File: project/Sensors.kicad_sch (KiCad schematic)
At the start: 19 parts, among them IC201 APDS-9306-065, IC202 BMI270, IC203 BMP581, IC204 LIS2MDLTR, IC205 BME688, Q201 DMG1013UW-7

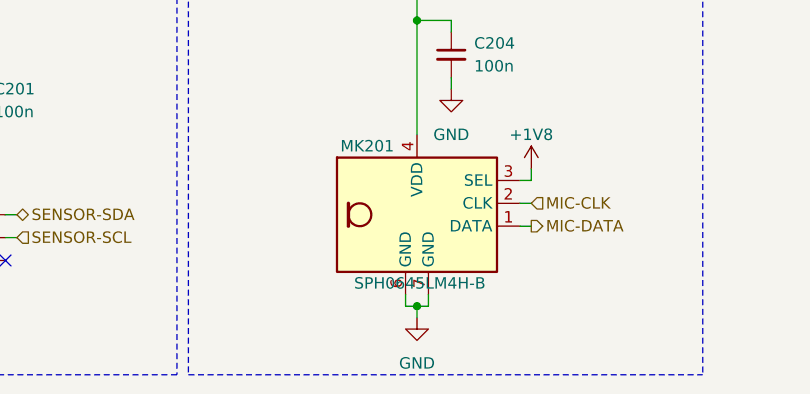
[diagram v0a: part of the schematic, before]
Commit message: Fix wrong value and datasheet for microphone
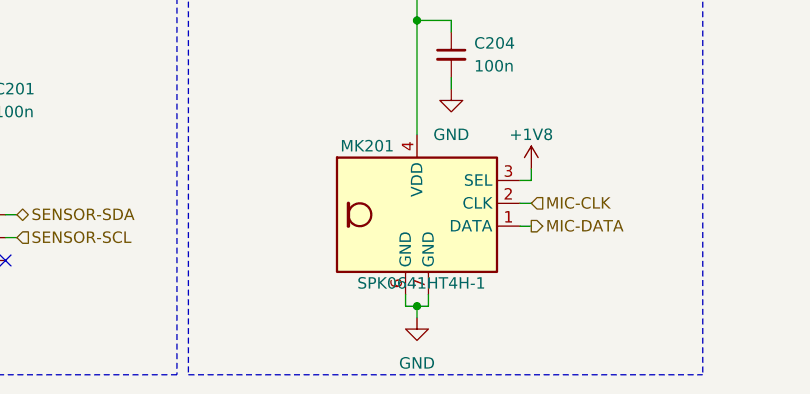
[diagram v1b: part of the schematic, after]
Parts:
- MK201: value SPH0645LM4H-B -> SPK0641HT4H-1
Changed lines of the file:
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@@
       (effects (font (size 1.27 1.27)) (justify right))
     )
-    (property "Value" "SPH0645LM4H-B" (at 87.63 186.69 0)
+    (property "Value" "SPK0641HT4H-1" (at 87.63 186.69 0)
       (effects (font (size 1.27 1.27)) (justify right))
     )
@@
       (effects (font (size 1.27 1.27)) hide)
     )
-    (property "Datasheet" "https://www.knowles.com/docs/default-source/default-document-library/sph0645lm4h-1-datasheet.pdf" (at 80.01 179.07 0)
+    (property "Datasheet" "https://www.knowles.com/docs/default-source/model-downloads/spk0641ht4h-1-rev-a.pdf" (at 80.01 179.07 0)
       (effects (font (size 1.27 1.27)) hide)
     )

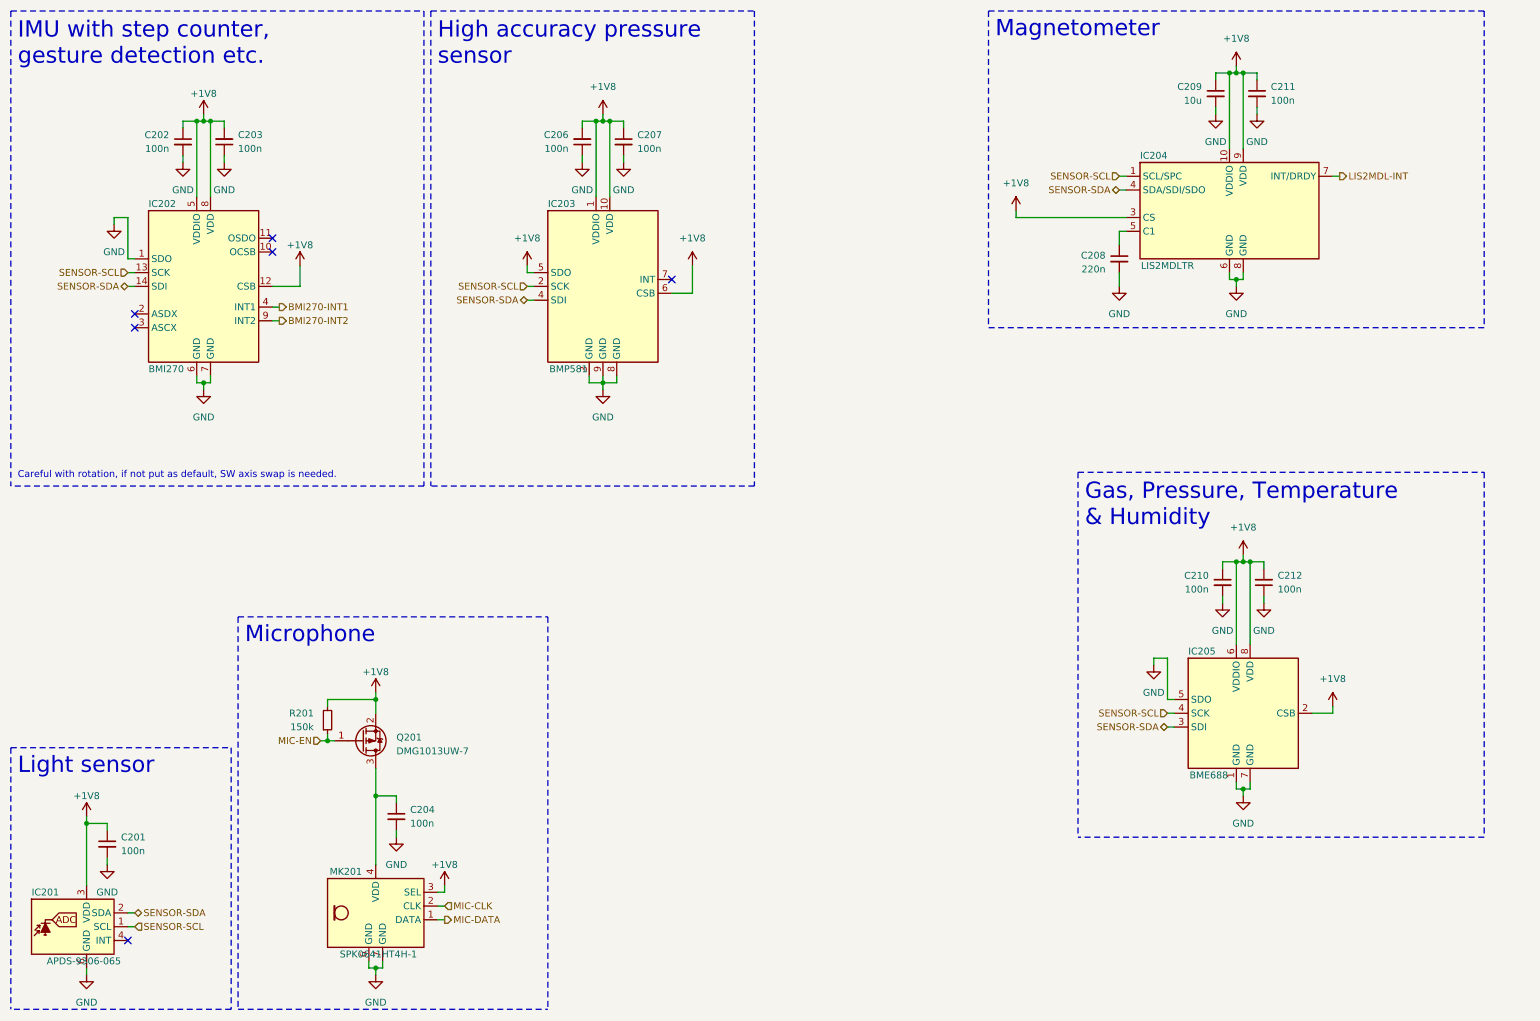
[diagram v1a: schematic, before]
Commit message: - Replace flash with MX25L51245GZ2I - Replace bridge resistors for SWD / USB switch with jumpers - Fix missing datasheets, update documentation - Fix wrong reset label at the dock connector - Add new logo
Signed-off-by: Daniel Kampert <DanielKampert@kampis-elektroecke.de>
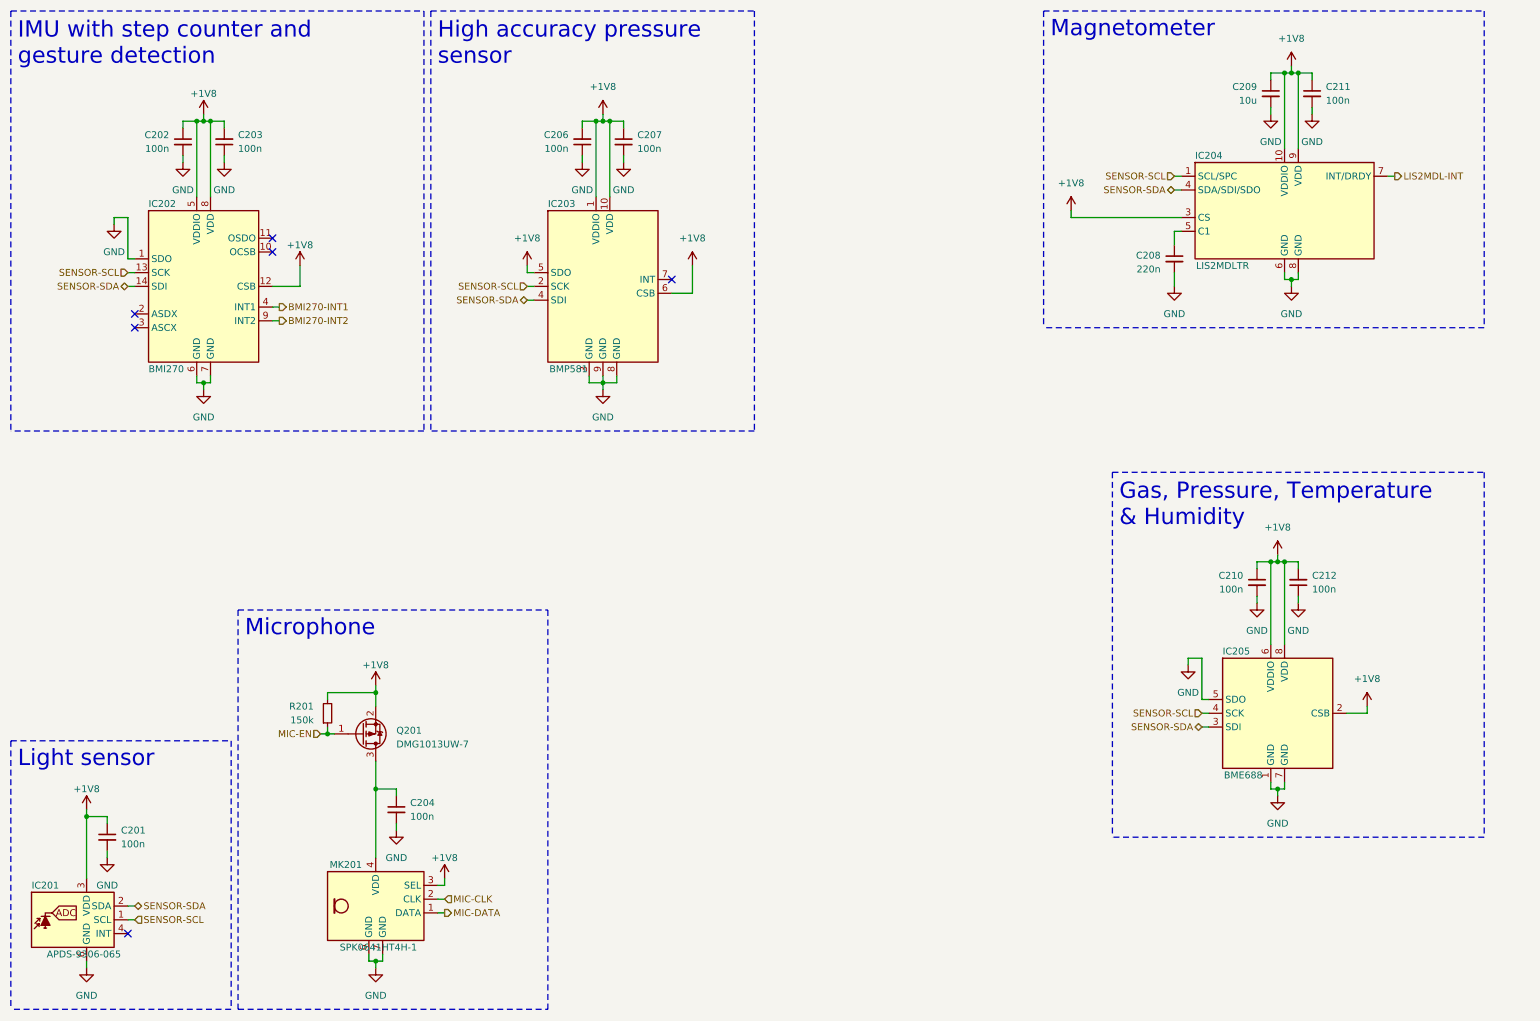
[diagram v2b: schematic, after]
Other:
- note added: "IMU with step counter and gesture detection"
- note removed: "Careful with rotation, if not put as default, SW axis swap is needed."
- note removed: "IMU with step counter, gesture detection etc."
- moved on the sheet: C201, C204, C208, C209, C210, C211, C212, IC201, IC204, IC205, MK201, Q201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
